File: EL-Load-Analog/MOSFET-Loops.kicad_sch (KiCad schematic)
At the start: 98 parts, among them Q201 2N7002, Q202 2N7002, Q203 IRFP250M, Q204 IRFP250M, Q205 2N7002, Q206 2N7002, Q207 IRFP250M, Q208 IRFP250M, U201 LM318D, U202 LM318D, U203 MCP6V51/LTC2050HV, U204 MCP6V51/LTC2050HV, U205 LM318D, U206 LM318D, U207 MCP6V51/LTC2050HV, U208 MCP6V51/LTC2050HV

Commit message: Major Analog PCB update DAC/ADC + connectors included, fan IC removed
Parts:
- removed NT203: NetTie_2, Jumper:SolderJumper-2_P1.3mm_Bridged_RoundedPad1.0x1.5mm, symbol Device:NetTie_2
- added F1: Fuse, Fuse:Fuseholder_Cylinder-5x20mm_Schurter_0031_8201_Horizontal_Open, symbol Device:Fuse
- added J2: Plus Terminal w. sense, Footprints:Deltron_Dual_4mm_572_0x00, symbol Connector:Conn_01x02_Socket
- added J5: Minus Terminal w. sense, Footprints:Deltron_Dual_4mm_572_0x00, symbol Connector:Conn_01x02_Socket
- added R23: 0, Resistor_SMD:R_0805_2012Metric, symbol Device:R_Small
- C201, C202, C203, C204, C205, C206, C207, C208, C209, C210, C211, C212, C213, C214, C215, C216, C217, C218, C219, C220, C221, C222, C223, C224, C225, C226, C227, C228: footprint Capacitor_SMD:C_0805_2012Metric_Pad1.18x1.45mm_HandSolder -> Capacitor_SMD:C_0805_2012Metric
- D201, D202, D204, D205, D206, D207, D208, D209: footprint Diode_SMD:D_MiniMELF_Handsoldering -> Diode_SMD:D_MiniMELF
- D203: value 1.5KE100A -> 1.5KE100A smd variant; footprint Diode_THT:D_DO-201AE_P15.24mm_Horizontal -> Diode_SMD:D_SMC
- H201, H202: footprint MountingHole:MountingHole_4.3mm_M4_Pad_Via -> MountingHole:MountingHole_4.3mm_M4_Pad_TopBottom
- NT201, NT202: footprint Jumper:SolderJumper-2_P1.3mm_Bridged_RoundedPad1.0x1.5mm -> NetTie:NetTie-2_SMD_Pad0.5mm
- R201, R202, R203, R204, R205, R206, R207, R208, R209, R210, R211, R212, R213, R214, R215, R216, R217, R218, R221, R222, R223, R224, R225, R226, R227, R228, R229, R230, R231, R232, R233, R234, R235, R236, R237, R238: footprint Resistor_SMD:R_0805_2012Metric_Pad1.20x1.40mm_HandSolder -> Resistor_SMD:R_0805_2012Metric
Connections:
- net -5VA is gone; now on net -5V: C202.1, C206.1, C216.1, C220.1, U201.4 (V-), U202.4 (V-), U205.4 (V-), U206.4 (V-)
- net GND: now also R23.2
- net LoadMin: now also J5.1 (Pin_1), R23.1
- net LoadPlus: now also F1.2; no longer H201.1, NT201.2
- new net LoadMinSense: J5.2 (Pin_2)
- new net LoadPlusSense: J2.2 (Pin_2)
- new net Plus: F1.1, H201.1, J2.1 (Pin_1), NT201.2
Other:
- note added: "Alternative Terminals"
- moved on the sheet: H201, H202, NT201, NT202

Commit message: Added snubber on input, bananajacks, sense connector, some cleanup.
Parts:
- removed H201: Plus Terminal, MountingHole:MountingHole_4.3mm_M4_Pad_TopBottom, symbol Mechanical:MountingHole_Pad
- removed H202: Min Terminal, MountingHole:MountingHole_4.3mm_M4_Pad_TopBottom, symbol Mechanical:MountingHole_Pad
- removed J2: Plus Terminal w. sense, Footprints:Deltron_Dual_4mm_572_0x00, symbol Connector:Conn_01x02_Socket
- removed J5: Minus Terminal w. sense, Footprints:Deltron_Dual_4mm_572_0x00, symbol Connector:Conn_01x02_Socket
- added C3: 100nF, Capacitor_THT:C_Rect_L18.0mm_W5.0mm_P15.00mm_FKS3_FKP3, symbol Device:C
- added J2, J5: Conn_01x01_MountingPin, EL-Load-Analog:SWEB-8094-AU, symbol Connector_Generic_MountingPin:Conn_01x01_MountingPin
- added J7: Conn_01x02_Socket, Connector_Phoenix_MC:PhoenixContact_MC_1,5_2-G-3.81_1x02_P3.81mm_Horizontal, symbol Connector:Conn_01x02_Socket
- added R2: 1k5 (2W), Resistor_THT:R_Axial_DIN0516_L15.5mm_D5.0mm_P5.08mm_Vertical, symbol Device:R
- C209, C210, C211, C212, C223, C224, C225, C226: now not fitted
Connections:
- net GND: now also J2.MP (MountPin)
- net LoadMin: now also J2.1 (Pin_1), R2.1
- net LoadMinSense: now also J7.2 (Pin_2)
- net LoadPlus: now also C3.1
- net LoadPlusSense: now also J7.1 (Pin_1)
- net Plus: no longer names the net of F1.1, NT201.2
- net Plus: now also J5.1 (Pin_1)
- new net: C3.2, R2.2
- no-connect marks 12 -> 13
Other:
- note added: "Snubber network to filter transient spikes f-3db = 1kHz"
- note removed: "Alternative Terminals"

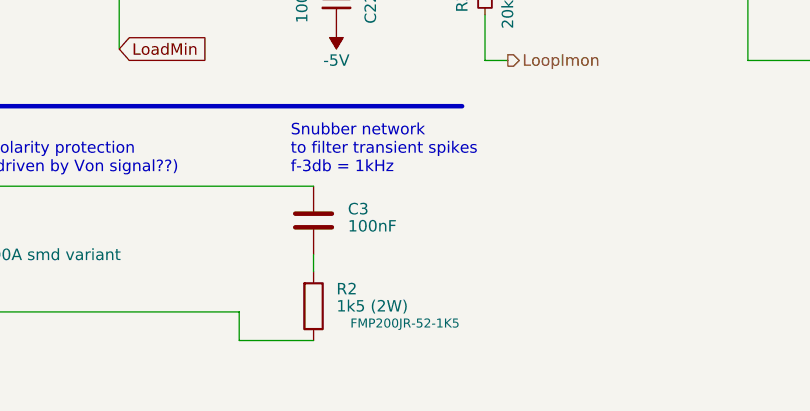
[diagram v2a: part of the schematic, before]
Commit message: Added SenseError detection (including ocmponents), added clearances, fixed few BOM items.
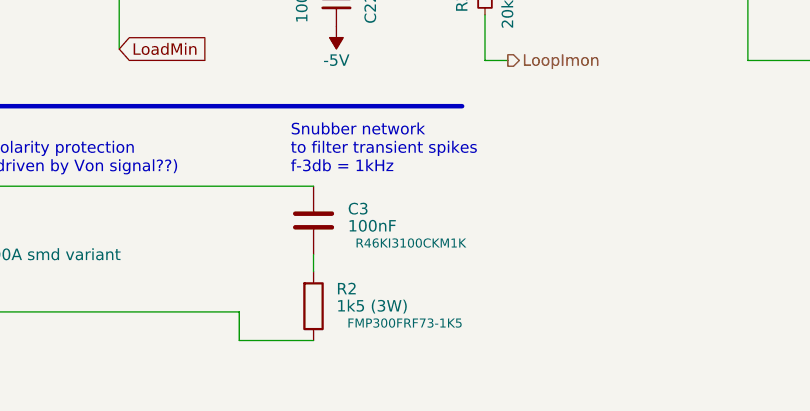
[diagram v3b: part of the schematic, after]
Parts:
- C201, C202, C203, C204, C205, C206, C207, C208, C215, C216, C217, C218, C219, C220, C221, C222: Part Name (none) -> C_100.0nF_0805_20%
- C209, C210, C223, C224: Part Name (none) -> C_4.7nF_0805_20%; now left out of the parts list
- C211, C212, C225, C226: Part Name (none) -> C_470.0pF_0805_20%; now left out of the parts list
- C213, C214, C227, C228: Part Name (none) -> C_470.0pF_0805_20%
- C3: MPN (none) -> R46KI3100CKM1K; Part Name (none) -> C_100.0nF_15mm_THT_X2_10%
- D201, D202, D204, D205, D206, D207, D208, D209: Part Name (none) -> D_Z_16V_miniMELF
- D203: Part Name (none) -> D_1.5KE100A_SMC
- J2: value Conn_01x01_MountingPin -> SWEB8094AU-SW; Part Name (none) -> H_Banana_Socket_24A_Black
- J5: value Conn_01x01_MountingPin -> SWEB8094AU-RT; Part Name (none) -> H_Banana_Socket_24A_Red
- J7: Part Name (none) -> H_Plug_2P_3.81MM_PCB_HOR
- Q201, Q202, Q205, Q206: Part Name (none) -> Q_2N7002
- Q203, Q204, Q207, Q208: Part Name (none) -> Q_IRFP250MPBF
- R2: value 1k5 (2W) -> 1k5 (3W); MPN FMP200JR-52-1K5 -> FMP300FRF73-1K5; Part Name (none) -> R_1.5kΩ_THT_15mm_5mm_3W_1%
- R201, R202, R221, R222: Part Name (none) -> R_10.0kΩ_0805_1%
- R203, R205, R223, R225: Part Name (none) -> R_100.0kΩ_0805_1%
- R204, R206, R224, R226: Part Name (none) -> R_20k_0805_0.1%
- R207, R208, R227, R228: Part Name (none) -> R_100.0Ω_0805_1%
- R209, R210, R229, R230: Part Name (none) -> R_1.0MΩ_0805_1%
- R211, R212, R213, R214, R231, R232, R233, R234: Part Name (none) -> R_100k_0805_0.1%
- R215, R216, R217, R218, R235, R236, R237, R238: Part Name (none) -> R_1k1_0805_0.1%
- R219, R220, R239, R240: Part Name (none) -> R_R01_2512_1%_20ppmC
- R23: Part Name (none) -> R_0.0Ω_0805_1%
- U201, U202, U205, U206: Part Name (none) -> U_LM318D
- U203, U204, U207, U208: Part Name (none) -> U_LTC2050HVCS5
